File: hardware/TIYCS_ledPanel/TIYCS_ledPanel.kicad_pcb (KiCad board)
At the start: 2 copper layers, 203 x 203 mm, 444 parts

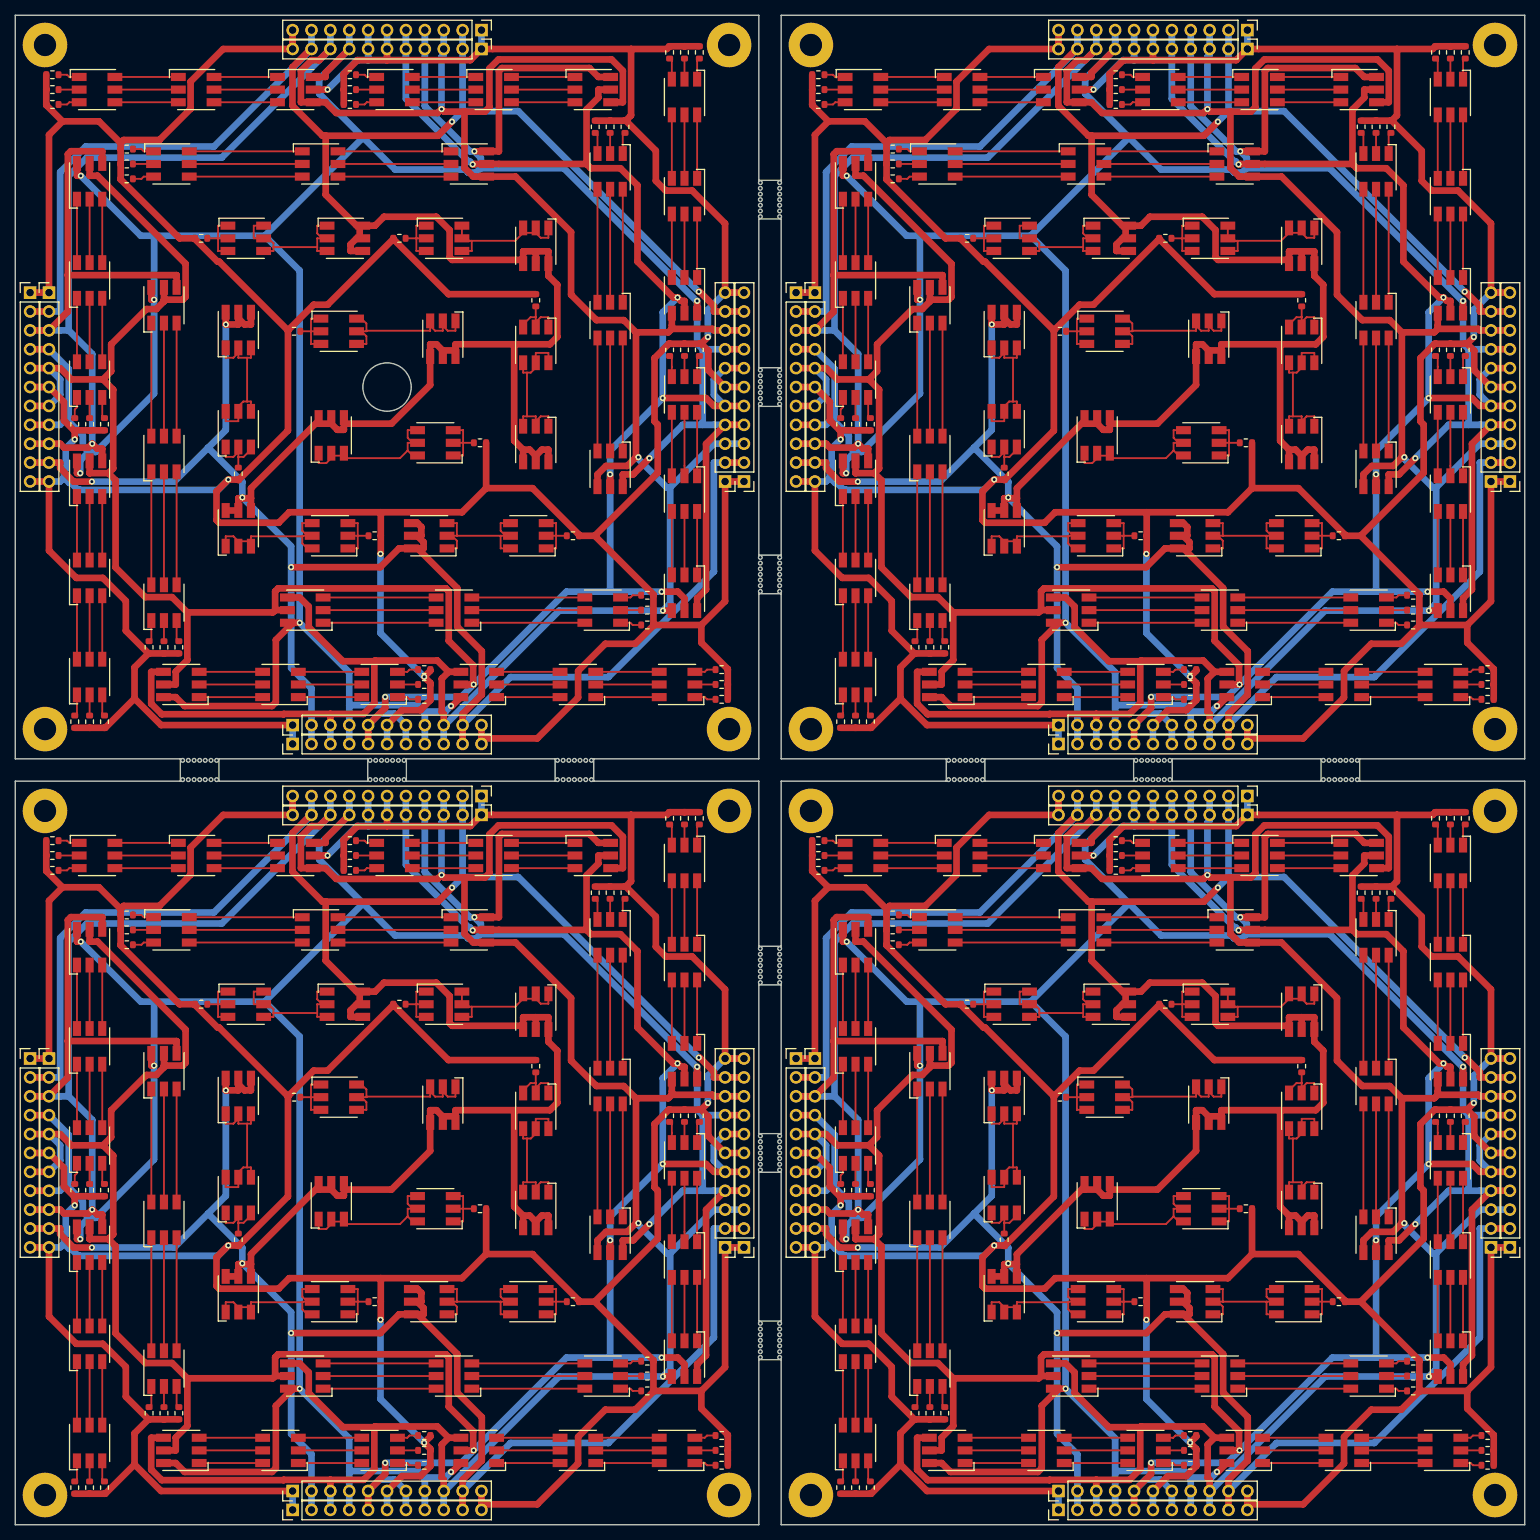
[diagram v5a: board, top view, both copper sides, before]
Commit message: PPCL-2 footprint for white LEDs
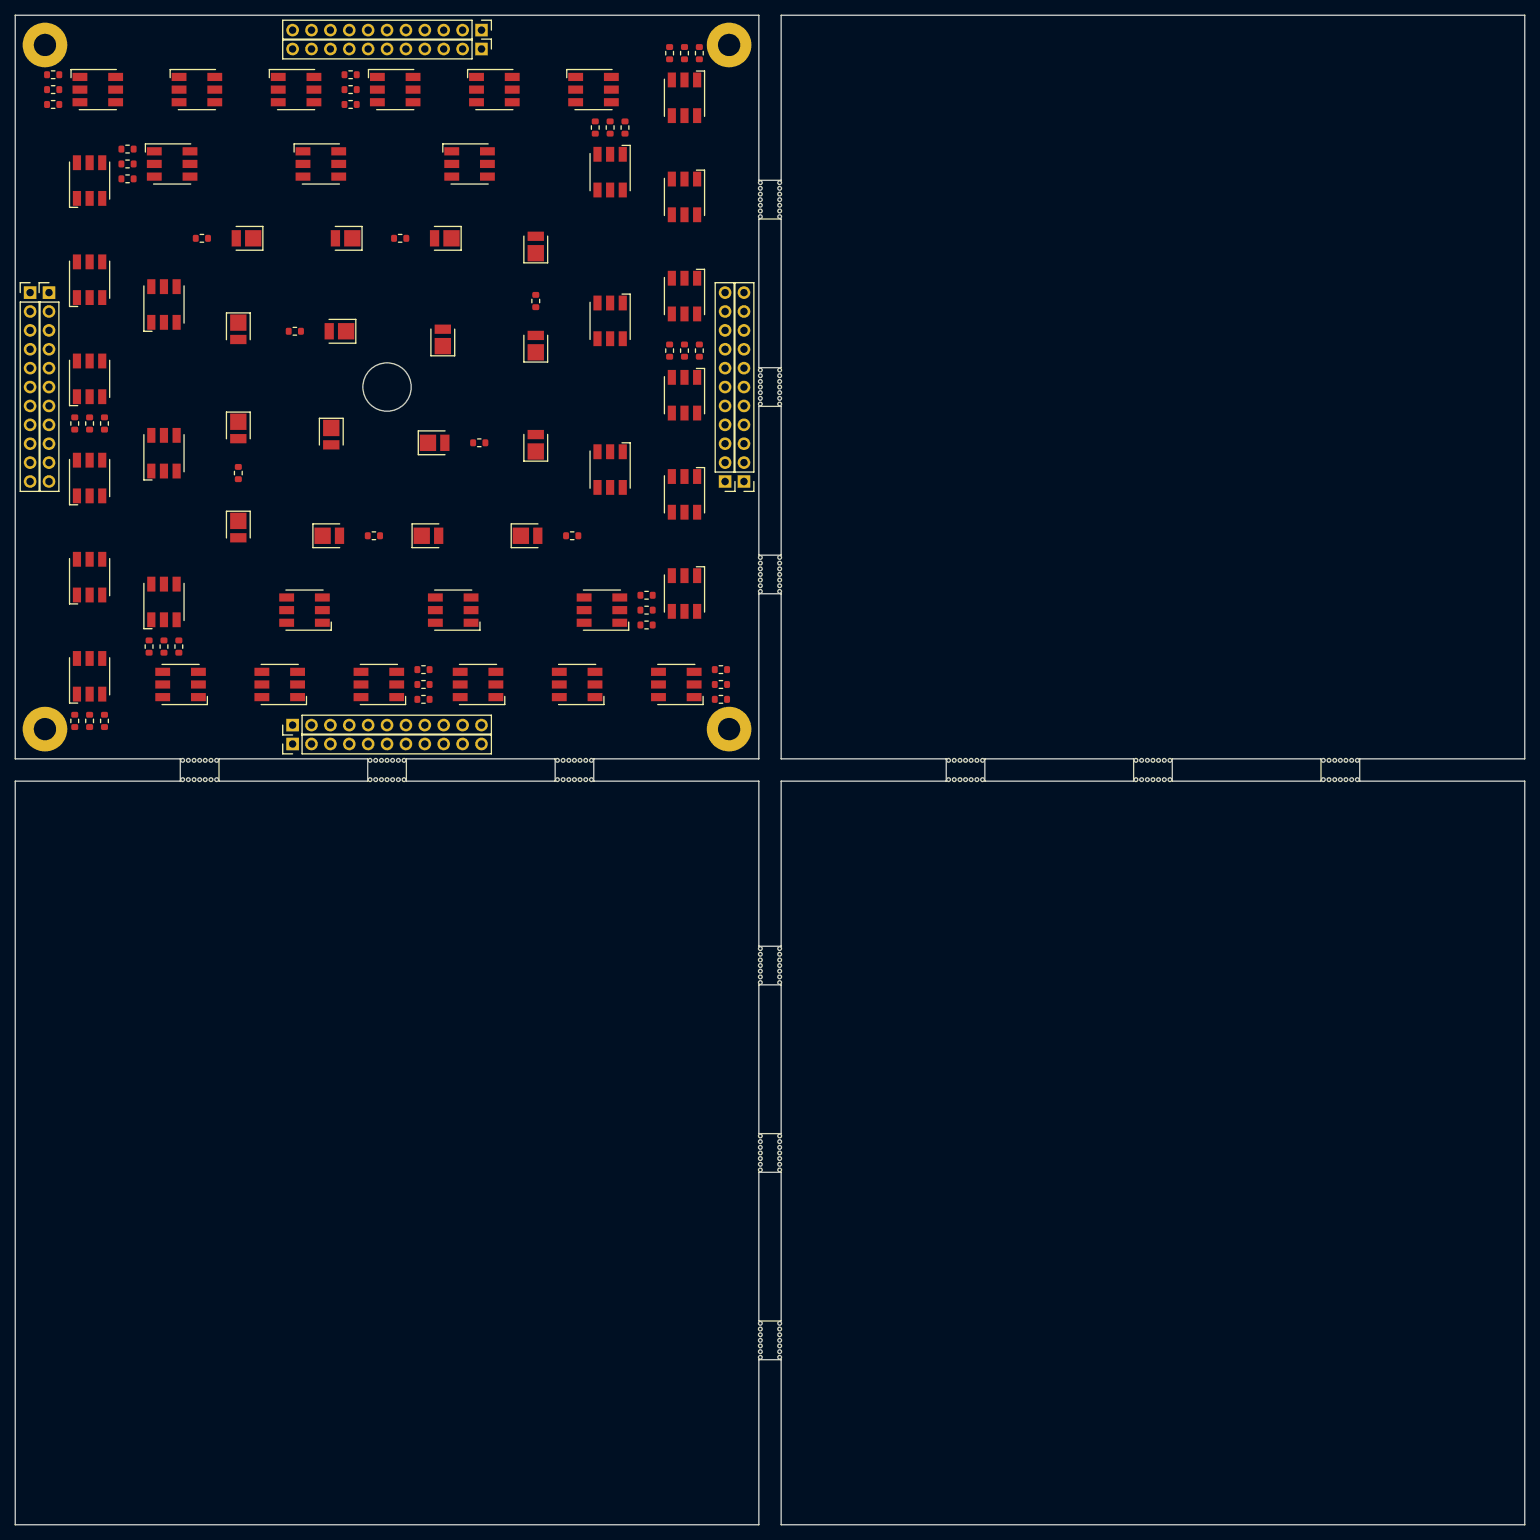
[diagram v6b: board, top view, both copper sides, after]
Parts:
- removed H_10, H_11, H_12, H_13, H_14, H_15, H_4, H_5, H_6, H_7, H_8, H_9: MountingHole_3mm_Pad, MountingHole_3mm_Pad
- removed LED_RGB2_12, LED_RGB2_13, LED_RGB2_14, LED_RGB2_15, LED_RGB2_16, LED_RGB2_17, LED_RGB2_18, LED_RGB2_19, LED_RGB2_20, LED_RGB2_21, LED_RGB2_22, LED_RGB2_23, LED_RGB2_24, LED_RGB2_25, LED_RGB2_26, LED_RGB2_27, LED_RGB2_28, LED_RGB2_29, LED_RGB2_30, LED_RGB2_31, LED_RGB2_32, LED_RGB2_33, LED_RGB2_34, LED_RGB2_35, LED_RGB2_36, LED_RGB2_37, LED_RGB2_38, LED_RGB2_39, LED_RGB2_40, LED_RGB2_41, LED_RGB2_42, LED_RGB2_43, LED_RGB2_44, LED_RGB2_45, LED_RGB2_46, LED_RGB2_47, LED_RGB_24, LED_RGB_25, LED_RGB_26, LED_RGB_27, LED_RGB_28, LED_RGB_29, LED_RGB_30, LED_RGB_31, LED_RGB_32, LED_RGB_33, LED_RGB_34, LED_RGB_35, LED_RGB_36, LED_RGB_37, LED_RGB_38, LED_RGB_39, LED_RGB_40, LED_RGB_41, LED_RGB_42, LED_RGB_43, LED_RGB_44, LED_RGB_45, LED_RGB_46, LED_RGB_47, LED_RGB_48, LED_RGB_49, LED_RGB_50, LED_RGB_51, LED_RGB_52, LED_RGB_53, LED_RGB_54, LED_RGB_55, LED_RGB_56, LED_RGB_57, LED_RGB_58, LED_RGB_59, LED_RGB_60, LED_RGB_61, LED_RGB_62, LED_RGB_63, LED_RGB_64, LED_RGB_65, LED_RGB_66, LED_RGB_67, LED_RGB_68, LED_RGB_69, LED_RGB_70, LED_RGB_71, LED_RGB_72, LED_RGB_73, LED_RGB_74, LED_RGB_75, LED_RGB_76, LED_RGB_77, LED_RGB_78, LED_RGB_79, LED_RGB_80, LED_RGB_81, LED_RGB_82, LED_RGB_83, LED_RGB_84, LED_RGB_85, LED_RGB_86, LED_RGB_87, LED_RGB_88, LED_RGB_89, LED_RGB_90, LED_RGB_91, LED_RGB_92, LED_RGB_93, LED_RGB_94, LED_RGB_95, LED_W2_10, LED_W2_11, LED_W2_12, LED_W2_13, LED_W2_14, LED_W2_15, LED_W2_4, LED_W2_5, LED_W2_6, LED_W2_7, LED_W2_8, LED_W2_9, LED_W_12, LED_W_13, LED_W_14, LED_W_15, LED_W_16, LED_W_17, LED_W_18, LED_W_19, LED_W_20, LED_W_21, LED_W_22, LED_W_23, LED_W_24, LED_W_25, LED_W_26, LED_W_27, LED_W_28, LED_W_29, LED_W_30, LED_W_31, LED_W_32, LED_W_33, LED_W_34, LED_W_35, LED_W_36, LED_W_37, LED_W_38, LED_W_39, LED_W_40, LED_W_41, LED_W_42, LED_W_43, LED_W_44, LED_W_45, LED_W_46, LED_W_47: LED_RGB_5050-6, LED_RGB_5050-6
- removed R_0_0_RGB1, R_0_0_RGB3, R_0_0_RGB4, R_0_0_RGB5, R_0_0_RGB6, R_0_0_RGB7, R_0_0_W1, R_0_0_W3, R_0_0_W4, R_0_0_W5, R_0_0_W6, R_0_0_W7, R_0_1_RGB1, R_0_1_RGB3, R_0_1_RGB4, R_0_1_RGB5, R_0_1_RGB6, R_0_1_RGB7, R_0_2_RGB1, R_0_2_RGB3, R_0_2_RGB4, R_0_2_RGB5, R_0_2_RGB6, R_0_2_RGB7, R_10_0_W1, R_10_0_W2, R_10_0_W3, R_12_0_RGB1, R_12_0_RGB2, R_12_0_RGB3, R_12_1_RGB1, R_12_1_RGB2, R_12_1_RGB3, R_12_2_RGB1, R_12_2_RGB2, R_12_2_RGB3, R_15_0_RGB1, R_15_0_RGB2, R_15_0_RGB3, R_15_1_RGB1, R_15_1_RGB2, R_15_1_RGB3, R_15_2_RGB1, R_15_2_RGB2, R_15_2_RGB3, R_18_0_RGB1, R_18_0_RGB2, R_18_0_RGB3, R_18_1_RGB1, R_18_1_RGB2, R_18_1_RGB3, R_18_2_RGB1, R_18_2_RGB2, R_18_2_RGB3, R_21_0_RGB1, R_21_0_RGB2, R_21_0_RGB3, R_21_1_RGB1, R_21_1_RGB2, R_21_1_RGB3, R_21_2_RGB1, R_21_2_RGB2, R_21_2_RGB3, R_2_0_W1, R_2_0_W3, R_2_0_W4, R_2_0_W5, R_2_0_W6, R_2_0_W7, R_3_0_RGB1, R_3_0_RGB3, R_3_0_RGB4, R_3_0_RGB5, R_3_0_RGB6, R_3_0_RGB7, R_3_1_RGB1, R_3_1_RGB3, R_3_1_RGB4, R_3_1_RGB5, R_3_1_RGB6, R_3_1_RGB7, R_3_2_RGB1, R_3_2_RGB3, R_3_2_RGB4, R_3_2_RGB5, R_3_2_RGB6, R_3_2_RGB7, R_4_0_W1, R_4_0_W2, R_4_0_W3, R_6_0_RGB1, R_6_0_RGB3, R_6_0_RGB4, R_6_0_RGB5, R_6_0_RGB6, R_6_0_RGB7, R_6_0_W1, R_6_0_W2, R_6_0_W3, R_6_1_RGB1, R_6_1_RGB3, R_6_1_RGB4, R_6_1_RGB5, R_6_1_RGB6, R_6_1_RGB7, R_6_2_RGB1, R_6_2_RGB3, R_6_2_RGB4, R_6_2_RGB5, R_6_2_RGB6, R_6_2_RGB7, R_8_0_W1, R_8_0_W2, R_8_0_W3, R_9_0_RGB1, R_9_0_RGB3, R_9_0_RGB4, R_9_0_RGB5, R_9_0_RGB6, R_9_0_RGB7, R_9_1_RGB1, R_9_1_RGB3, R_9_1_RGB4, R_9_1_RGB5, R_9_1_RGB6, R_9_1_RGB7, R_9_2_RGB1, R_9_2_RGB3, R_9_2_RGB4, R_9_2_RGB5, R_9_2_RGB6, R_9_2_RGB7: R_0603_1608Metric, R_0603_1608Metric
- removed mainConn_0_2, mainConn_0_3, mainConn_0_4, mainConn_0_5, mainConn_0_6, mainConn_0_7, mainConn_1_2, mainConn_1_3, mainConn_1_4, mainConn_1_5, mainConn_1_6, mainConn_1_7, mainConn_2_2, mainConn_2_3, mainConn_2_4, mainConn_2_5, mainConn_2_6, mainConn_2_7, mainConn_3_2, mainConn_3_3, mainConn_3_4, mainConn_3_5, mainConn_3_6, mainConn_3_7: PinHeader_1x11_P2.54mm_Vertical, PinHeader_1x11_P2.54mm_Vertical
- removed mouseBite_121, mouseBite_213, mouseBite_261, mouseBite_293, mouseBite_333, mouseBite_498, mouseBite_617, mouseBite_688, mouseBite_746, mouseBite_776, mouseBite_923, mouseBite_944: mouseBiteCustom, mouseBiteCustom
- added mouseBite_183: mouseBiteCustom, mouseBiteCustom, F.Cu at (25.2, 51.5)
- added mouseBite_50: mouseBiteCustom, mouseBiteCustom, F.Cu at (128.2, 51.5)
- added mouseBite_556: mouseBiteCustom, mouseBiteCustom, F.Cu at (51.5, 77.8)
- added mouseBite_603: mouseBiteCustom, mouseBiteCustom, F.Cu at (51.5, 25.2)
- added mouseBite_608: mouseBiteCustom, mouseBiteCustom, F.Cu at (0.00, 51.5)
- added mouseBite_633: mouseBiteCustom, mouseBiteCustom, F.Cu at (51.5, 128.2)
- added mouseBite_65: mouseBiteCustom, mouseBiteCustom, F.Cu at (-25.2, 51.5)
- added mouseBite_678: mouseBiteCustom, mouseBiteCustom, F.Cu at (51.5, 103.0)
- added mouseBite_693: mouseBiteCustom, mouseBiteCustom, F.Cu at (51.5, 0.00)
- added mouseBite_718: mouseBiteCustom, mouseBiteCustom, F.Cu at (103.0, 51.5)
- added mouseBite_735: mouseBiteCustom, mouseBiteCustom, F.Cu at (77.8, 51.5)
- added mouseBite_752: mouseBiteCustom, mouseBiteCustom, F.Cu at (51.5, -25.2)
- LED_W2_0, LED_W2_1, LED_W2_2, LED_W2_3, LED_W_0, LED_W_1, LED_W_10, LED_W_11, LED_W_2, LED_W_3, LED_W_4, LED_W_5, LED_W_6, LED_W_7, LED_W_8, LED_W_9: value LED_RGB_5050-6 -> LED_PLCC_2835; footprint LED_RGB_5050-6 -> LED_PLCC_2835
- moved R_10_0_W 0.10 mm to (-20.0, 11.6)
- moved R_4_0_W 0.10 mm to (20.0, -11.6)
- moved LED_W_1 0.10 mm to (-5.57, -20.0), turned to 180 degrees
- moved LED_W_10 0.10 mm to (-20.0, 5.57), turned to -90 degrees
- moved LED_W_4 0.10 mm to (20.0, -5.57), turned to 90 degrees
- moved LED_W_7 0.10 mm to (5.57, 20.0), turned to 0 degrees
- moved LED_RGB_1 0.10 mm to (-25.6, -40.0)
- moved LED_RGB_13 0.10 mm to (25.6, 40.0)
- moved LED_RGB_19 0.10 mm to (-40.0, 25.6)
- moved LED_RGB_7 0.10 mm to (40.0, -25.6)
- moved LED_RGB_10 0.10 mm to (40.0, 14.4)
- moved LED_RGB_16 0.10 mm to (-14.4, 40.0)
- moved LED_RGB_22 0.10 mm to (-40.0, -14.4)
- moved LED_RGB_4 0.10 mm to (14.4, -40.0)
- moved LED_RGB2_1 0.10 mm to (-8.90, -30.0)
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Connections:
- LED_W2_0 pad 1: RtoD0_W_2 -> D0toD1_W_2
- LED_W2_1 pad 1: D0toD1_W_2 -> W
- LED_W2_2 pad 1: RtoD2_W_2 -> D2toD3_W_2
- LED_W2_3 pad 1: D2toD3_W_2 -> W
- LED_W_0 pad 1: RtoD0_W_1 -> D0toD1_W_1
- LED_W_1 pad 1: D0toD1_W_1 -> W
- LED_W_10 pad 1: RtoD10_W_1 -> D10toD11_W_1
- LED_W_11 pad 1: D10toD11_W_1 -> W
- LED_W_2 pad 1: RtoD2_W_1 -> D2toD3_W_1
- LED_W_3 pad 1: D2toD3_W_1 -> W
- LED_W_4 pad 1: RtoD4_W_1 -> D4toD5_W_1
- LED_W_5 pad 1: D4toD5_W_1 -> W
- LED_W_6 pad 1: RtoD6_W_1 -> D6toD7_W_1
- LED_W_7 pad 1: D6toD7_W_1 -> W
- LED_W_8 pad 1: RtoD8_W_1 -> D8toD9_W_1
- LED_W_9 pad 1: D8toD9_W_1 -> W
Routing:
- net 12V: track 2641.0 -> 0.00 mm, vias 20 -> 0
- net W: track 2137.4 -> 0.00 mm, vias 24 -> 0
- net B: track 1875.6 -> 0.00 mm, vias 16 -> 0
- net G: track 1757.8 -> 0.00 mm, vias 32 -> 0
- net R: track 1594.8 -> 0.00 mm, vias 32 -> 0
- net D0toD1_W_2: track 95.0 -> 0.00 mm
- net D2toD3_W_2: track 90.3 -> 0.00 mm
- net D10toD11_W_1: track 87.4 -> 0.00 mm
- net D0toD1_W_1: track 87.4 -> 0.00 mm
- net D4toD5_W_1: track 87.4 -> 0.00 mm
- net D6toD7_W_1: track 84.7 -> 0.00 mm
- net D8toD9_W_1: track 84.6 -> 0.00 mm
- net D2toD3_W_1: track 78.1 -> 0.00 mm
- net D9toD10_Red_2: track 60.8 -> 0.00 mm
- net D9toD10_Green_2: track 60.8 -> 0.00 mm
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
